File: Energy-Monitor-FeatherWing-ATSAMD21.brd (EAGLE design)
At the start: 50.8 x 22.9 mm, 32 parts

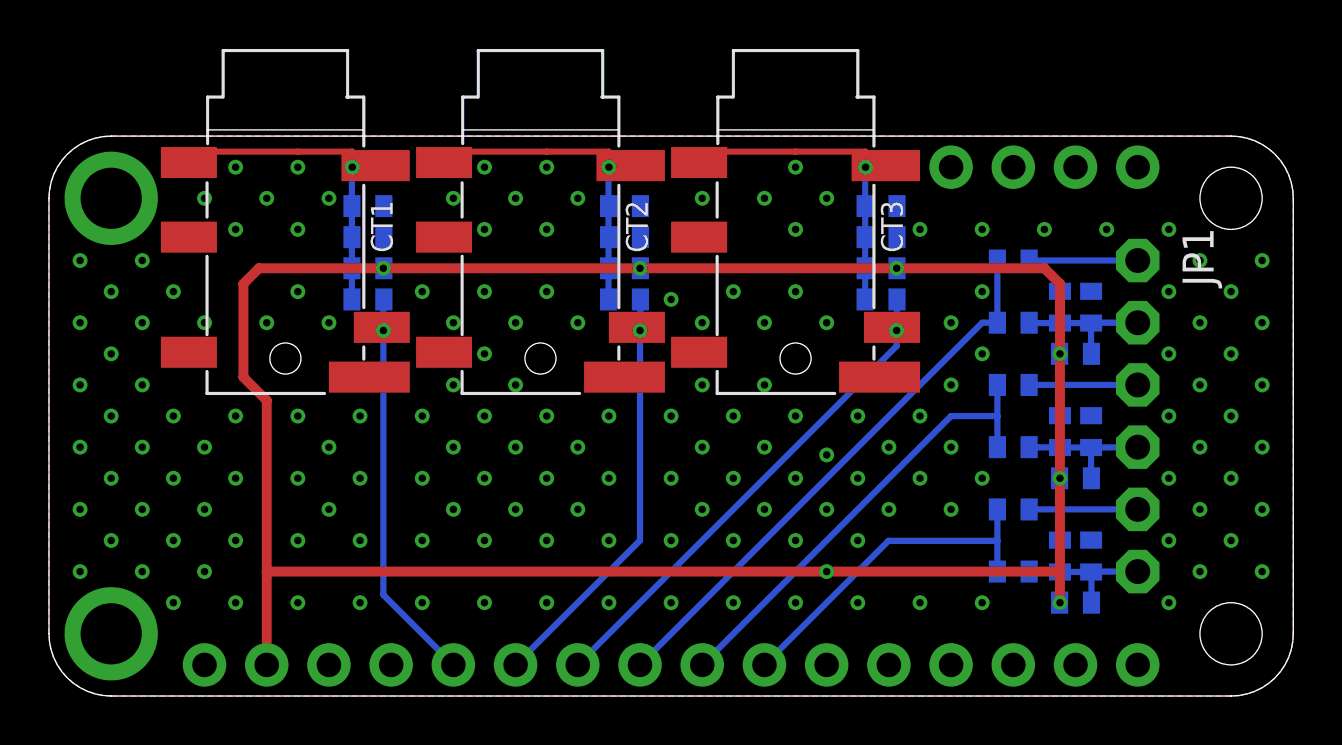
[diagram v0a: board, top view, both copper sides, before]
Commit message: Layout cleanup; add hints for PCBA
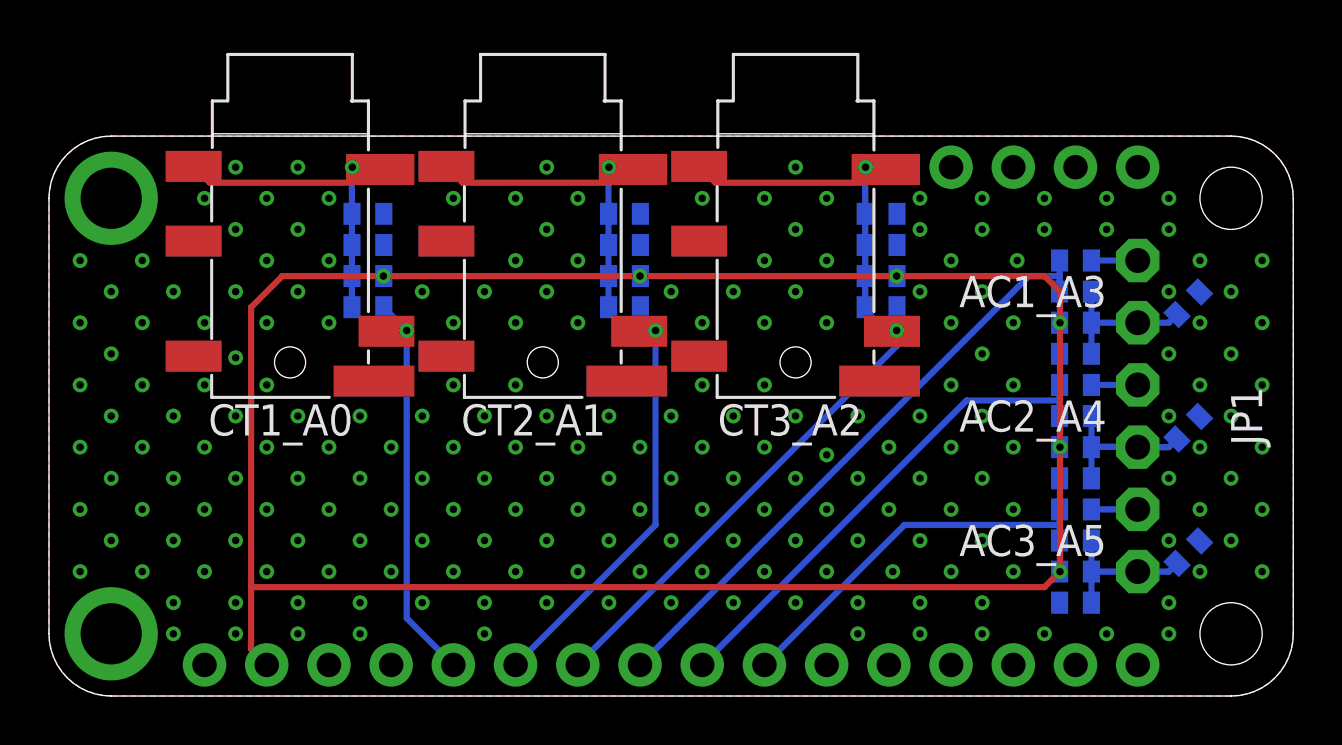
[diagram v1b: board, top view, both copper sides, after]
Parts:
- removed CT1, CT2, CT3: ST-PJ-312, ST-PJ-312:SUNTECH_ST-PJ-312
- added CT1_A0, CT2_A1, CT3_A2: ST-PJ-312, ST-PJ-312:SUNTECH_ST-PJ-312
- moved C4 3.97 mm to (46.5, 16.0), turned to 135 degrees
- moved C5 3.97 mm to (46.5, 11.0), turned to 135 degrees
- moved C6 3.97 mm to (46.5, 5.87), turned to 135 degrees
- moved R11 2.84 mm to (41.9, 16.5)
- moved R15 2.84 mm to (41.9, 11.4)
- moved R19 2.84 mm to (41.9, 6.35)
- moved R10 2.54 mm to (41.9, 17.8)
- moved R14 2.54 mm to (41.9, 12.7)
- moved R18 2.54 mm to (41.9, 7.62)
- moved R12 0.90 mm to (41.9, 15.2), turned to 180 degrees
- moved R16 0.90 mm to (41.9, 10.2), turned to 180 degrees
- moved R20 0.90 mm to (41.9, 5.08), turned to 180 degrees
- moved C1 0.32 mm to (13.0, 19.7)
- moved C2 0.32 mm to (23.5, 19.7)
- moved C3 0.32 mm to (34.0, 19.7)
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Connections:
- net AC_GND: now also R20.2, R21.1; no longer R20.1, R21.2
- net CT1_REF: now also CT1_A0.COM1, CT1_A0.COM2; no longer CT1.COM1, CT1.COM2
- net CT2_REF: now also CT2_A1.COM1, CT2_A1.COM2; no longer CT2.COM1, CT2.COM2
- net CT3_REF: now also CT3_A2.COM1, CT3_A2.COM2; no longer CT3.COM1, CT3.COM2
- net GND: now also CT1_A0.LS, CT2_A1.LS, CT3_A2.LS, R13.2, R17.2, R21.2; no longer CT1.LS, CT2.LS, CT3.LS, R12.2, R16.2, R20.2
- net N$1: now also CT1_A0.L; no longer CT1.L
- net N$2: now also CT2_A1.L; no longer CT2.L
- net N$3: now also CT3_A2.L; no longer CT3.L
- net N$6: now also R16.2, R17.1; no longer R16.1, R17.2
- net N$9: now also R12.2, R13.1; no longer R12.1, R13.2
- net VCC: now also R12.1, R16.1, R20.1; no longer R13.1, R17.1, R21.1
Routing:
- net VCC: track 98.2 -> 93.5 mm
- net N$7: track 4.43 -> 1.89 mm
- net N$4: track 4.43 -> 1.89 mm
- net N$10: track 4.43 -> 1.89 mm
- net N$5: track 22.9 -> 25.0 mm
- net N$11: track 14.1 -> 15.7 mm
- net N$8: track 18.8 -> 20.3 mm
- net N$1: track 16.5 -> 17.3 mm
- net N$2: track 17.2 -> 17.9 mm
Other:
- board text added: "10"
- board text added: "100k"
- board text added: "22"
- board text added: "470k"
- board text added: "AC1_A3"
- board text added: "AC2_A4"
- board text added: "AC3_A5"
